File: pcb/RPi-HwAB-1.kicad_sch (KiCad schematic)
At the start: 11 parts, among them J1 GPIO, J2 Hirose_FH12-16S, J3 TC2030, J4 Conn_ARM_SWD_TagConnect_TC203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, U1 XC7A35T-FGG484, U2 CAT24C256, U3 ADP5054

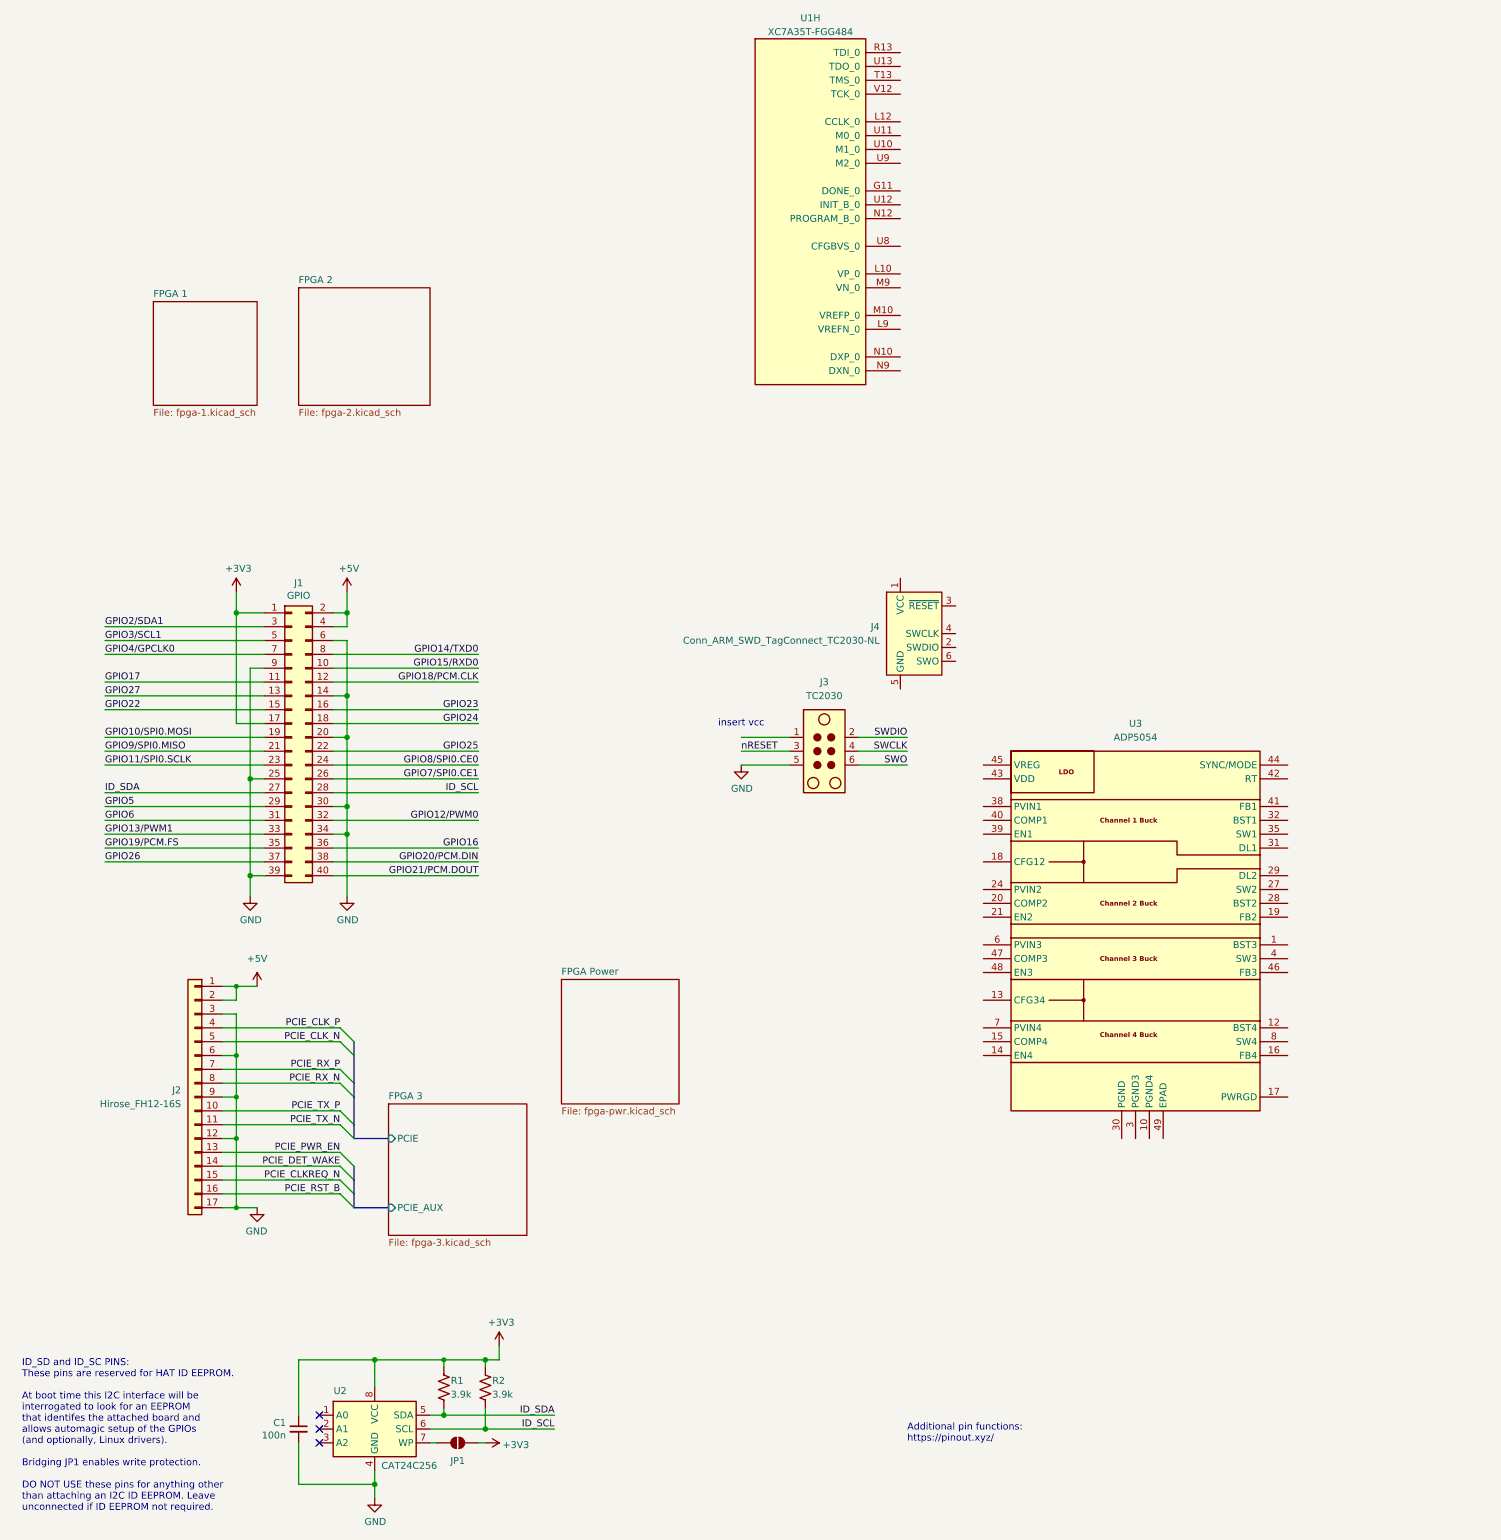
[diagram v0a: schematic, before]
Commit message: current sense, fpga power sequencing
plus restructuring files
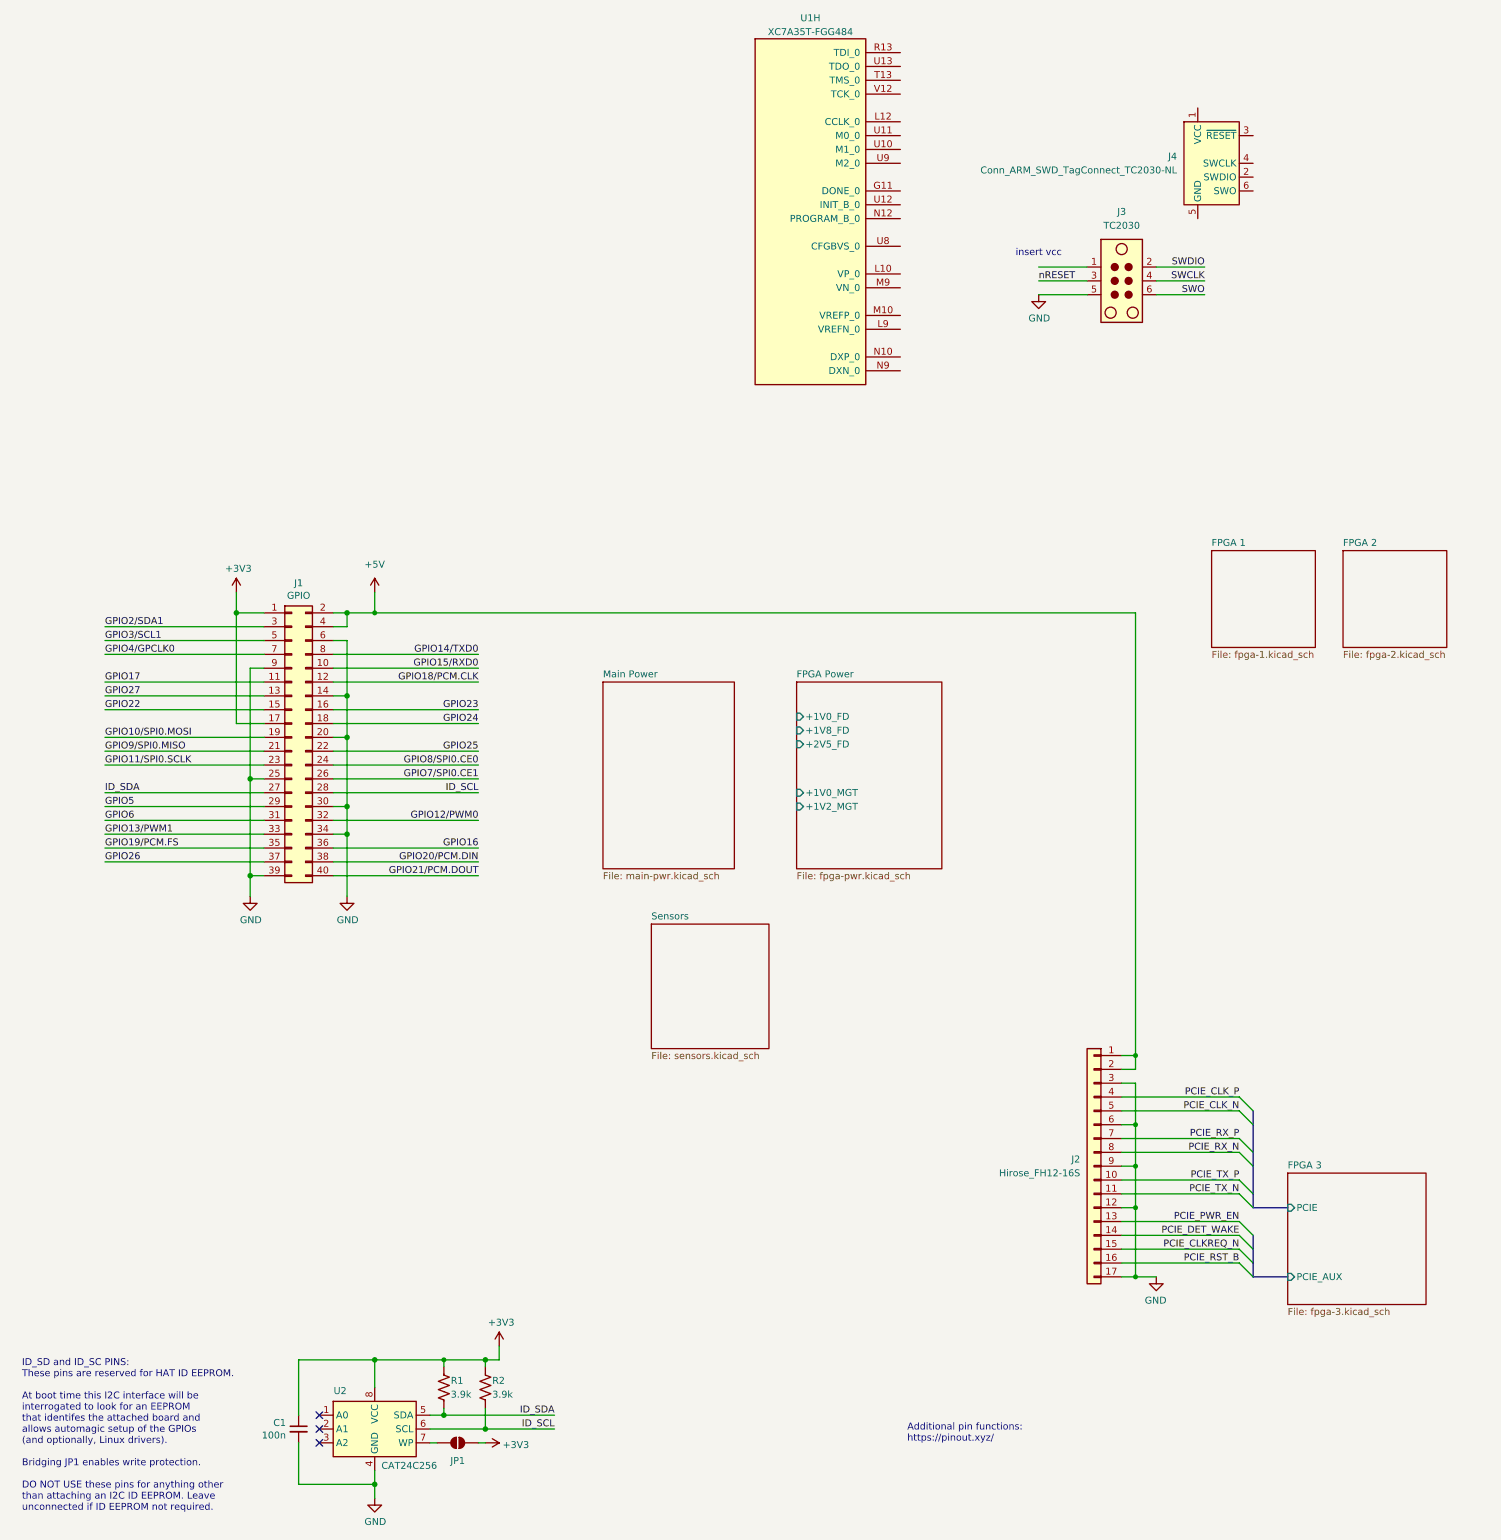
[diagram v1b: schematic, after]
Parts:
- removed U3: ADP5054, Package_DFN_QFN:QFN-48-1EP_7x7mm_P0.5mm_EP5.15x5.15mm, symbol Regulator_Switching:ADP5054
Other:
- added sheet Main Power (main-pwr.kicad_sch)
- added sheet Sensors (sensors.kicad_sch)
- sheet FPGA Power ports: added +1V0_FD, +1V0_MGT, +1V2_MGT, +1V8_FD, +2V5_FD; removed none
- moved on the sheet: J2, J3, J4

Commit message: add sensors, hierarchical changes
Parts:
- removed J3: TC2030, Connector:Tag-Connect_TC2030-IDC-NL_2x03_P1.27mm_Vertical, symbol Connector:TC2030
- removed J4: Conn_ARM_SWD_TagConnect_TC2030-NL, Connector:Tag-Connect_TC2030-IDC-NL_2x03_P1.27mm_Vertical, symbol Connector:Conn_ARM_SWD_TagConnect_TC2030-NL
- removed U1: XC7A35T-FGG484, Package_BGA:Xilinx_FGG484, symbol FPGA_Xilinx_Artix7:XC7A35T-FGG484
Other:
- added sheet Debug Connectors (debug.kicad_sch)
- note removed: "insert vcc"

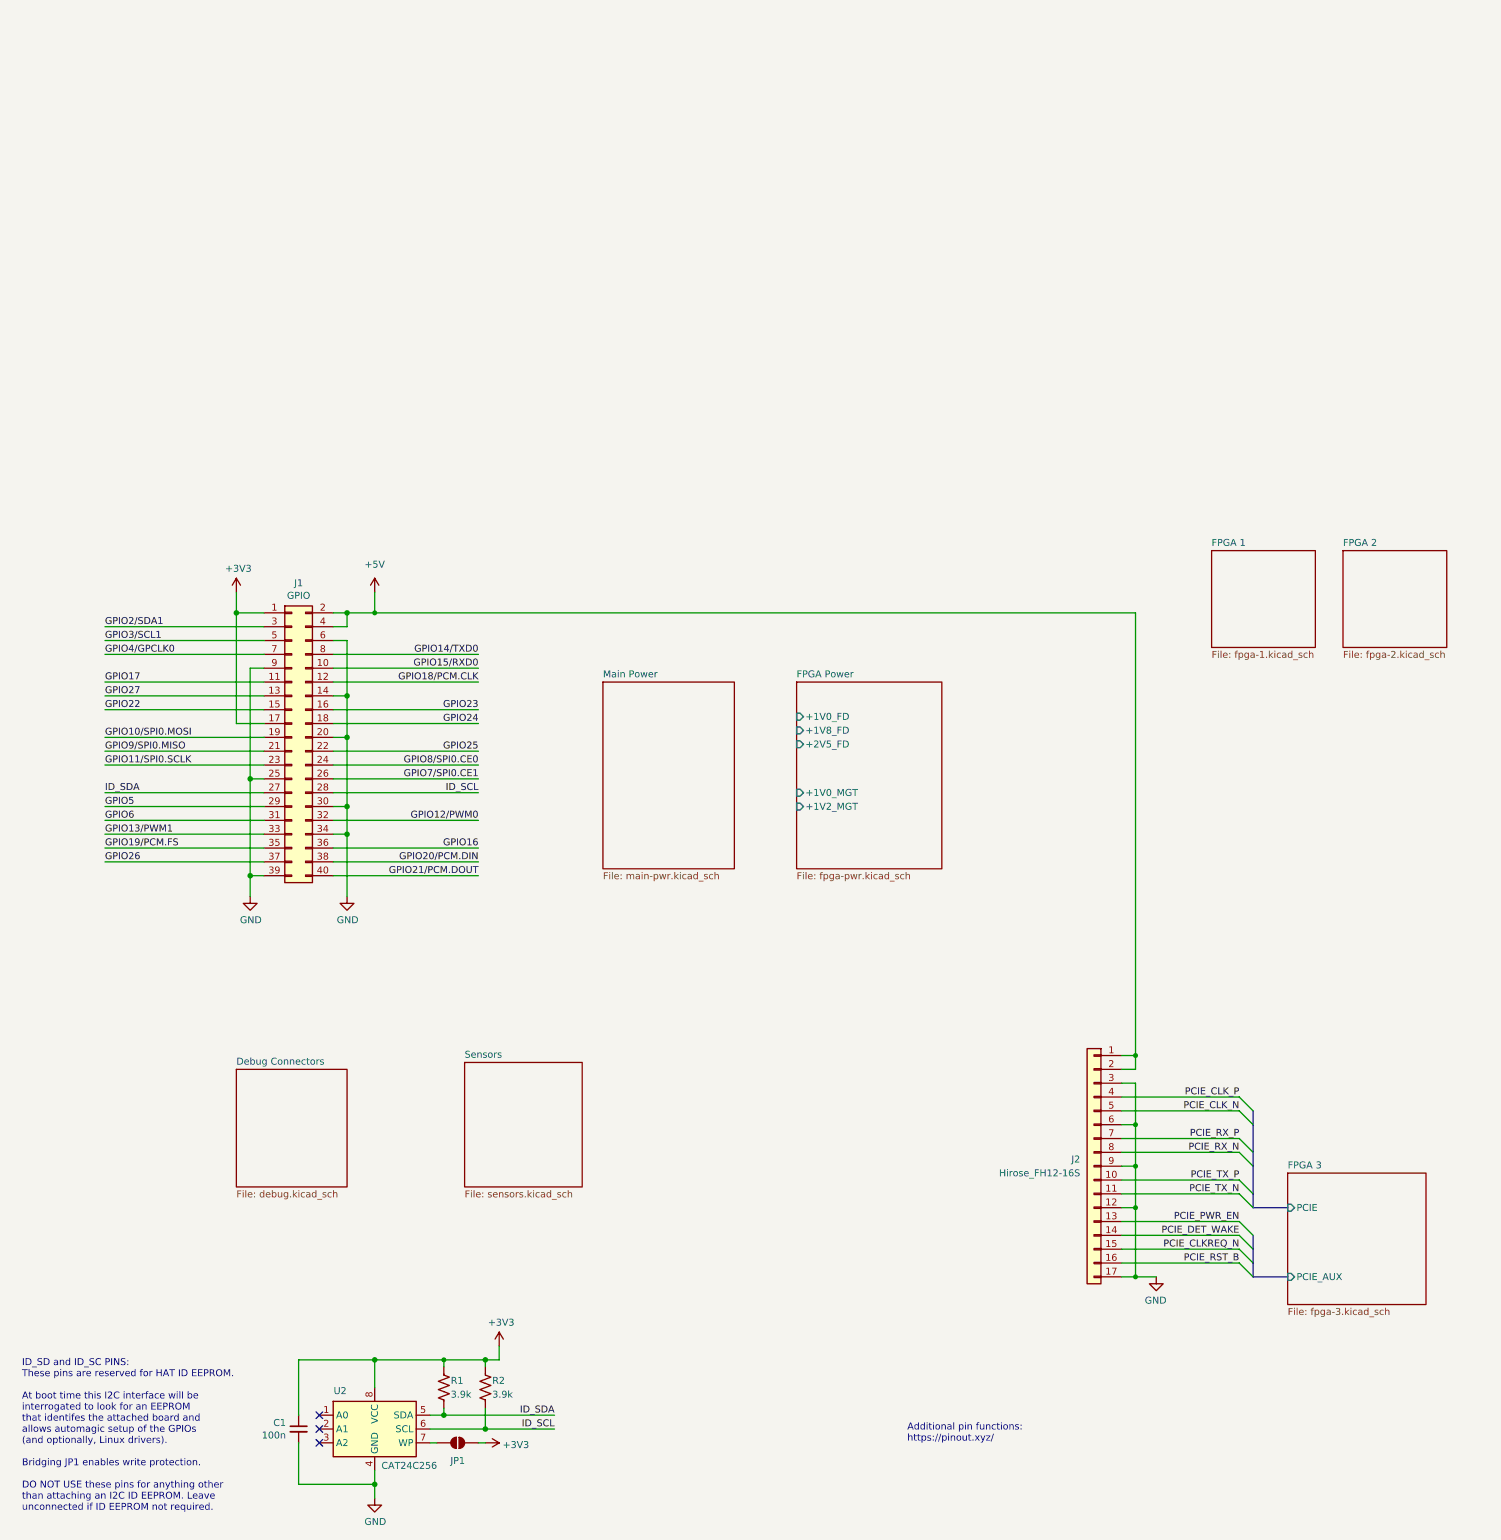
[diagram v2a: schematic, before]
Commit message: addl. updates to power hierarchy
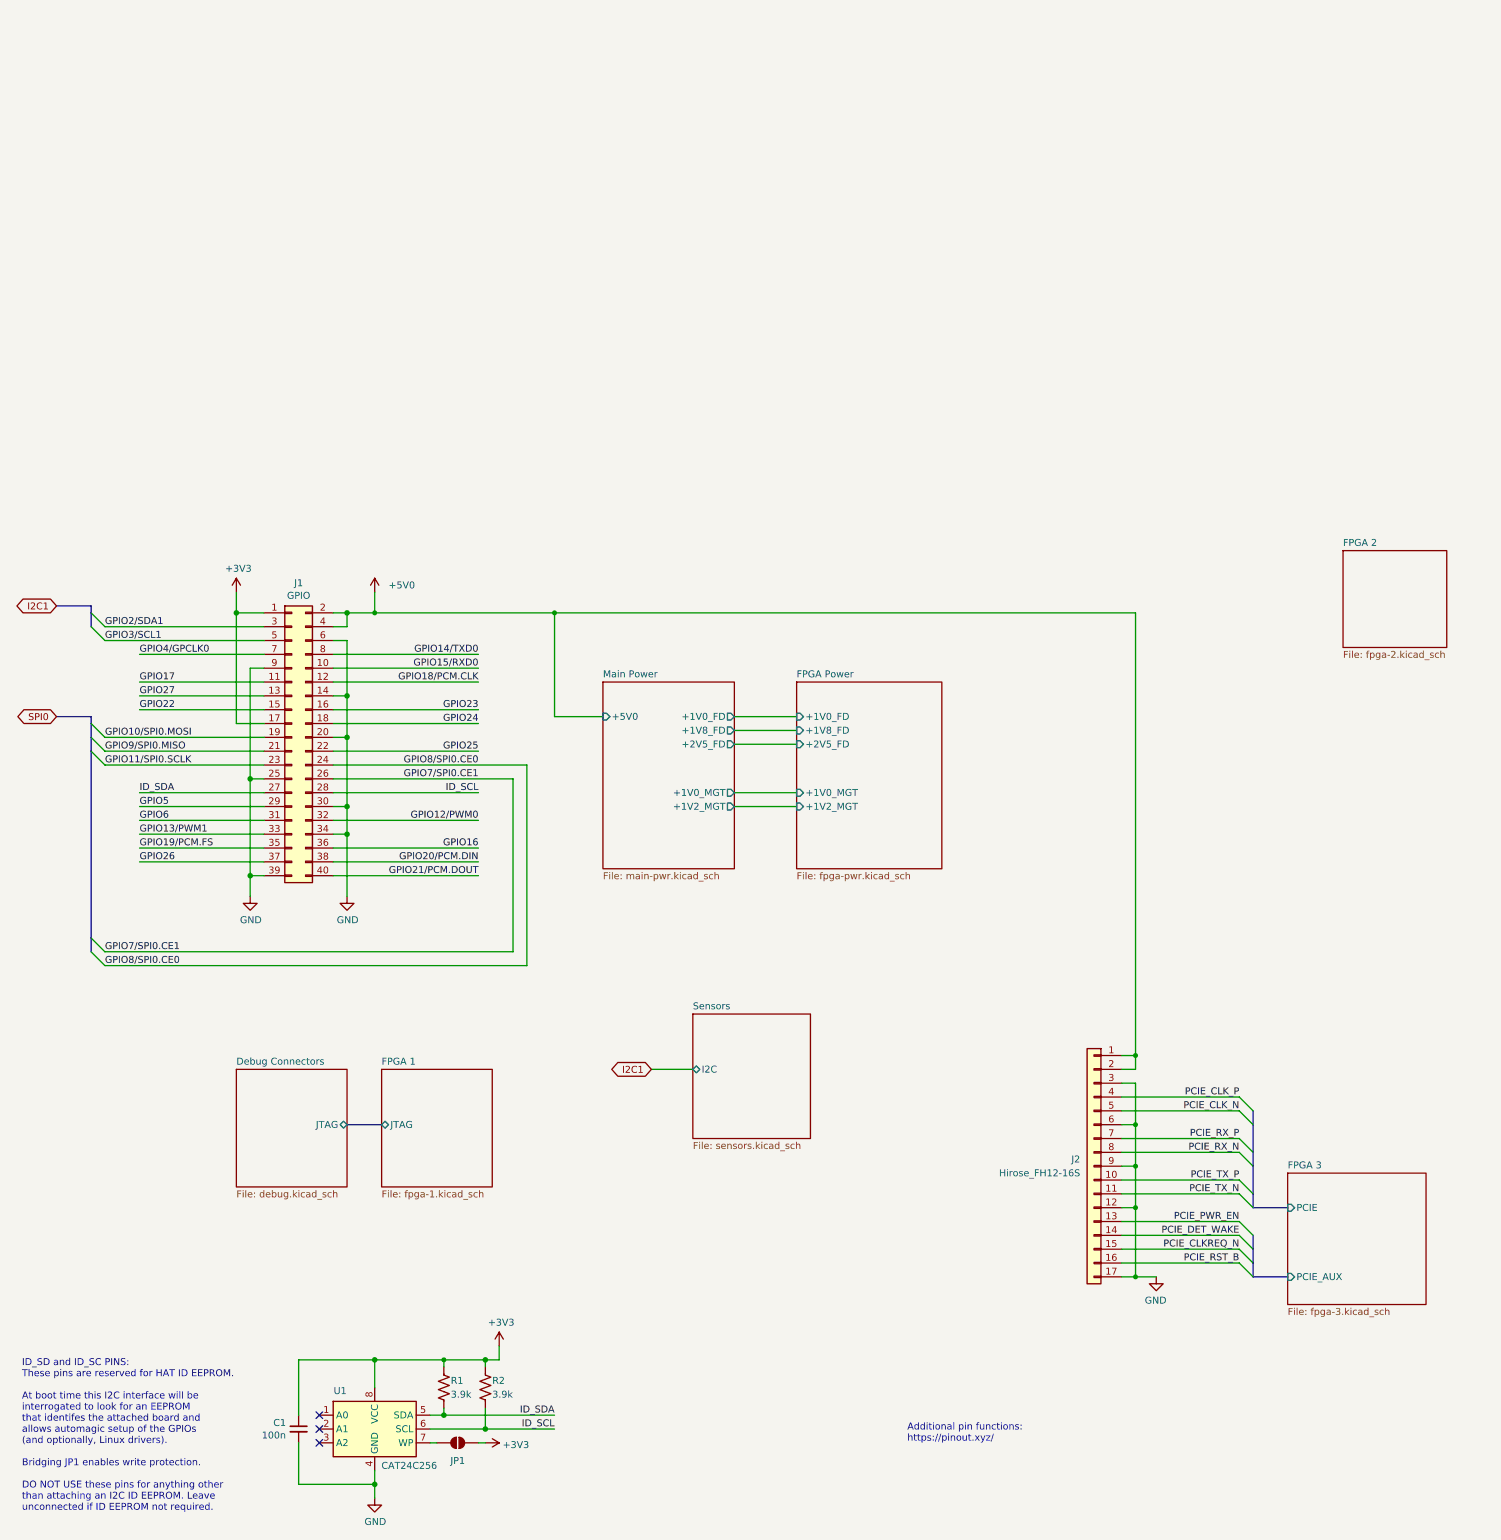
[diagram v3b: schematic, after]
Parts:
- renumbered U2 to U1
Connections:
- net +5V renamed +5V0
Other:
- sheet Debug Connectors ports: added JTAG; removed none
- sheet FPGA 1 ports: added JTAG; removed none
- sheet Main Power ports: added +1V0_FD, +1V0_MGT, +1V2_MGT, +1V8_FD, +2V5_FD, +5V0; removed none
- sheet Sensors ports: added I2C; removed none
